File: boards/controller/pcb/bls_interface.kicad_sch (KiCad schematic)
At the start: 5 parts, among them J1101 PWM, J1102 SPI, J1103 Power

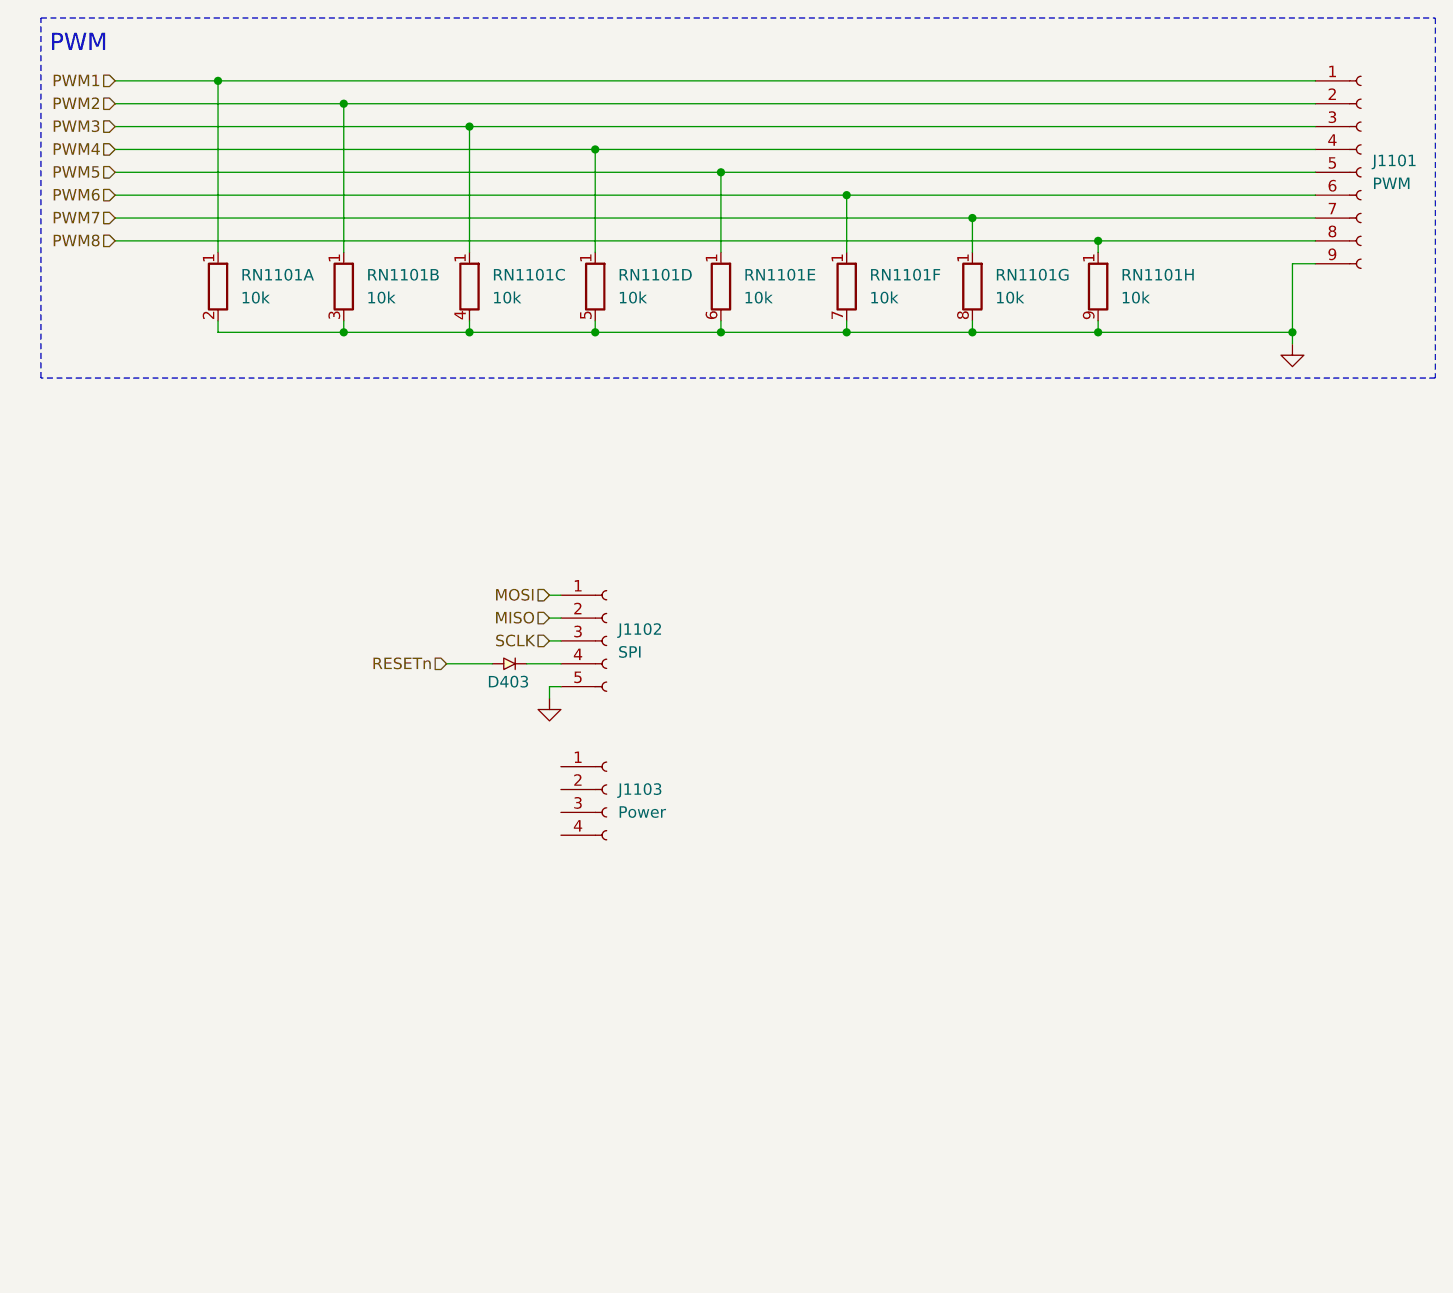
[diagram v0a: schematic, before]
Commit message: controller: pcb: Update schematic
Signed-off-by: Nicholas Loehrke <nicholasnloehrke@gmail.com>
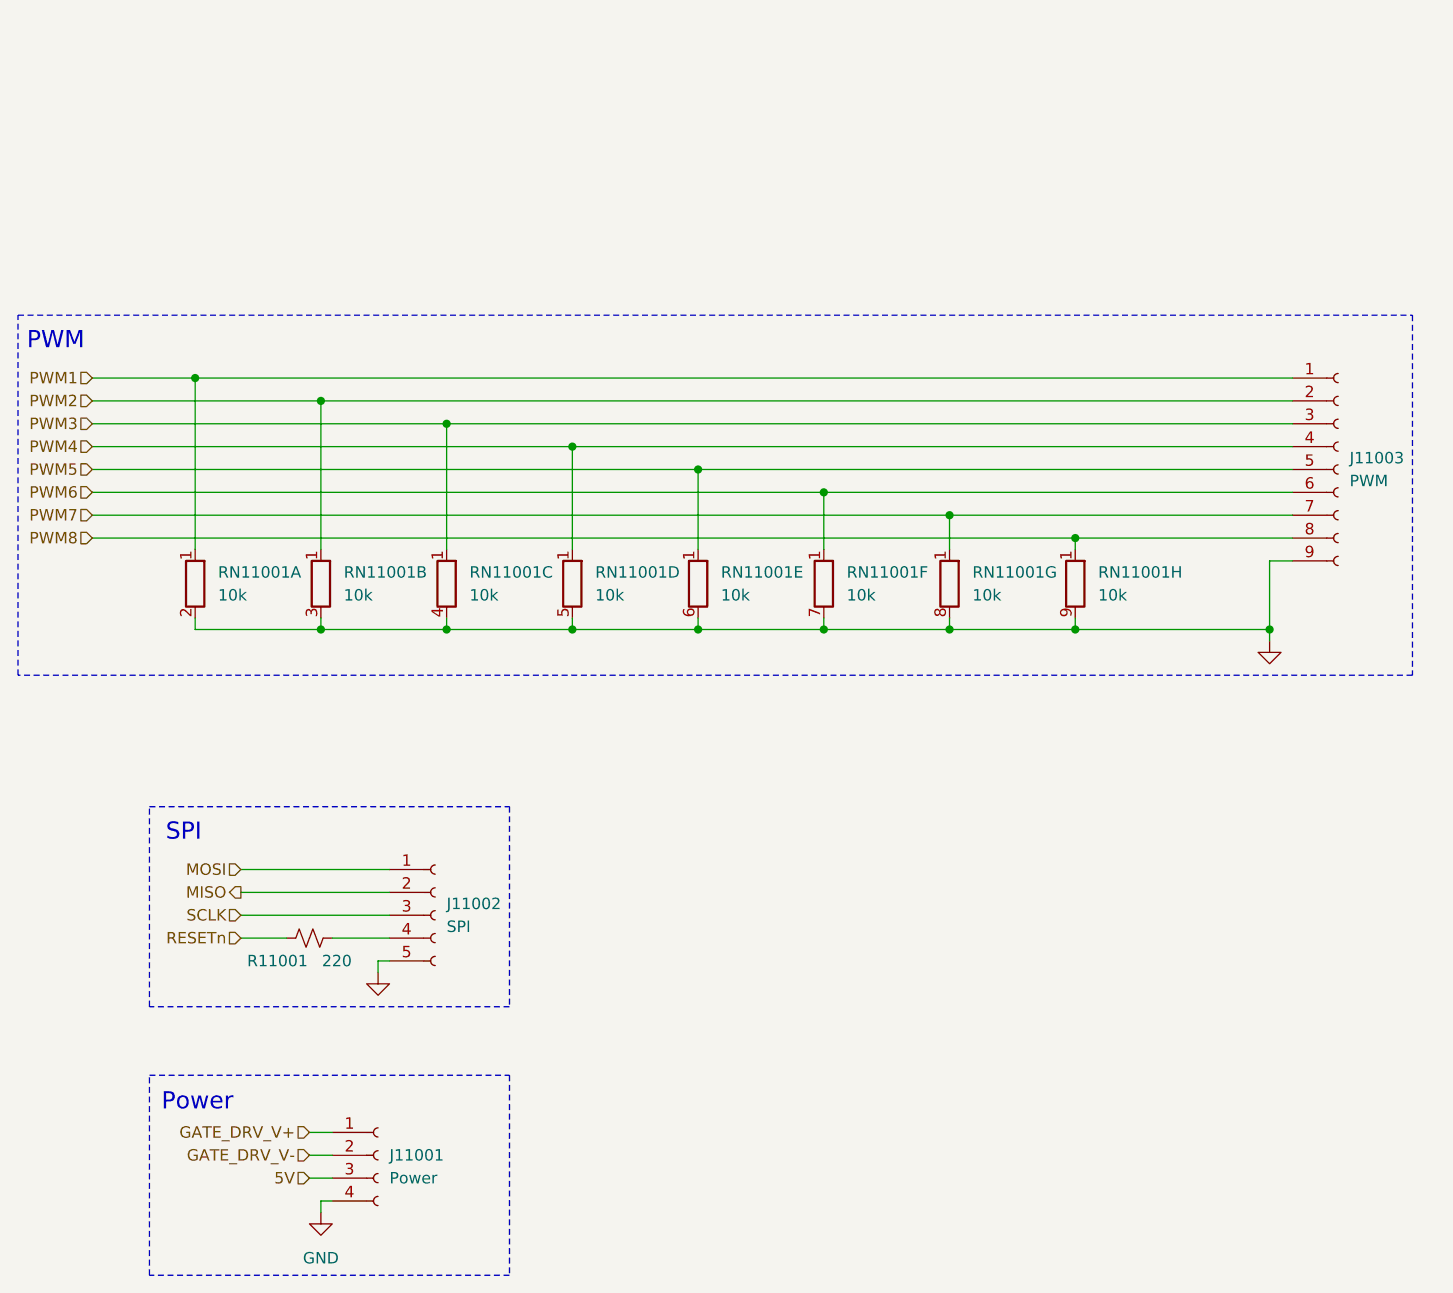
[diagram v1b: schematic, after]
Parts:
- removed D403: CUS10S30_H3F, USC_TOS, symbol CUS10S30_H3F:CUS10S30_H3F
- added R11001: 220, symbol Device:R_Small_US
- renumbered J1103 to J11001, J1102 to J11002, J1101 to J11003, RN1101 to RN11001
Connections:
- net GND: now also J11001.4 (Pin_4)
- net RESETn: now also R11001.1
- net GATE_DRV_V+: now reaches J11001.1 (Pin_1)
- net GATE_DRV_V-: now reaches J11001.2 (Pin_2)
- net 5V: now reaches J11001.3 (Pin_3)
- net at J11002.4 (Pin_4): now also R11001.2
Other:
- note added: "Power"
- note added: "SPI"
- moved on the sheet: J11001, J11002, J11003, RN11001A, RN11001B, RN11001C, RN11001D, RN11001E, RN11001F, RN11001G, RN11001H

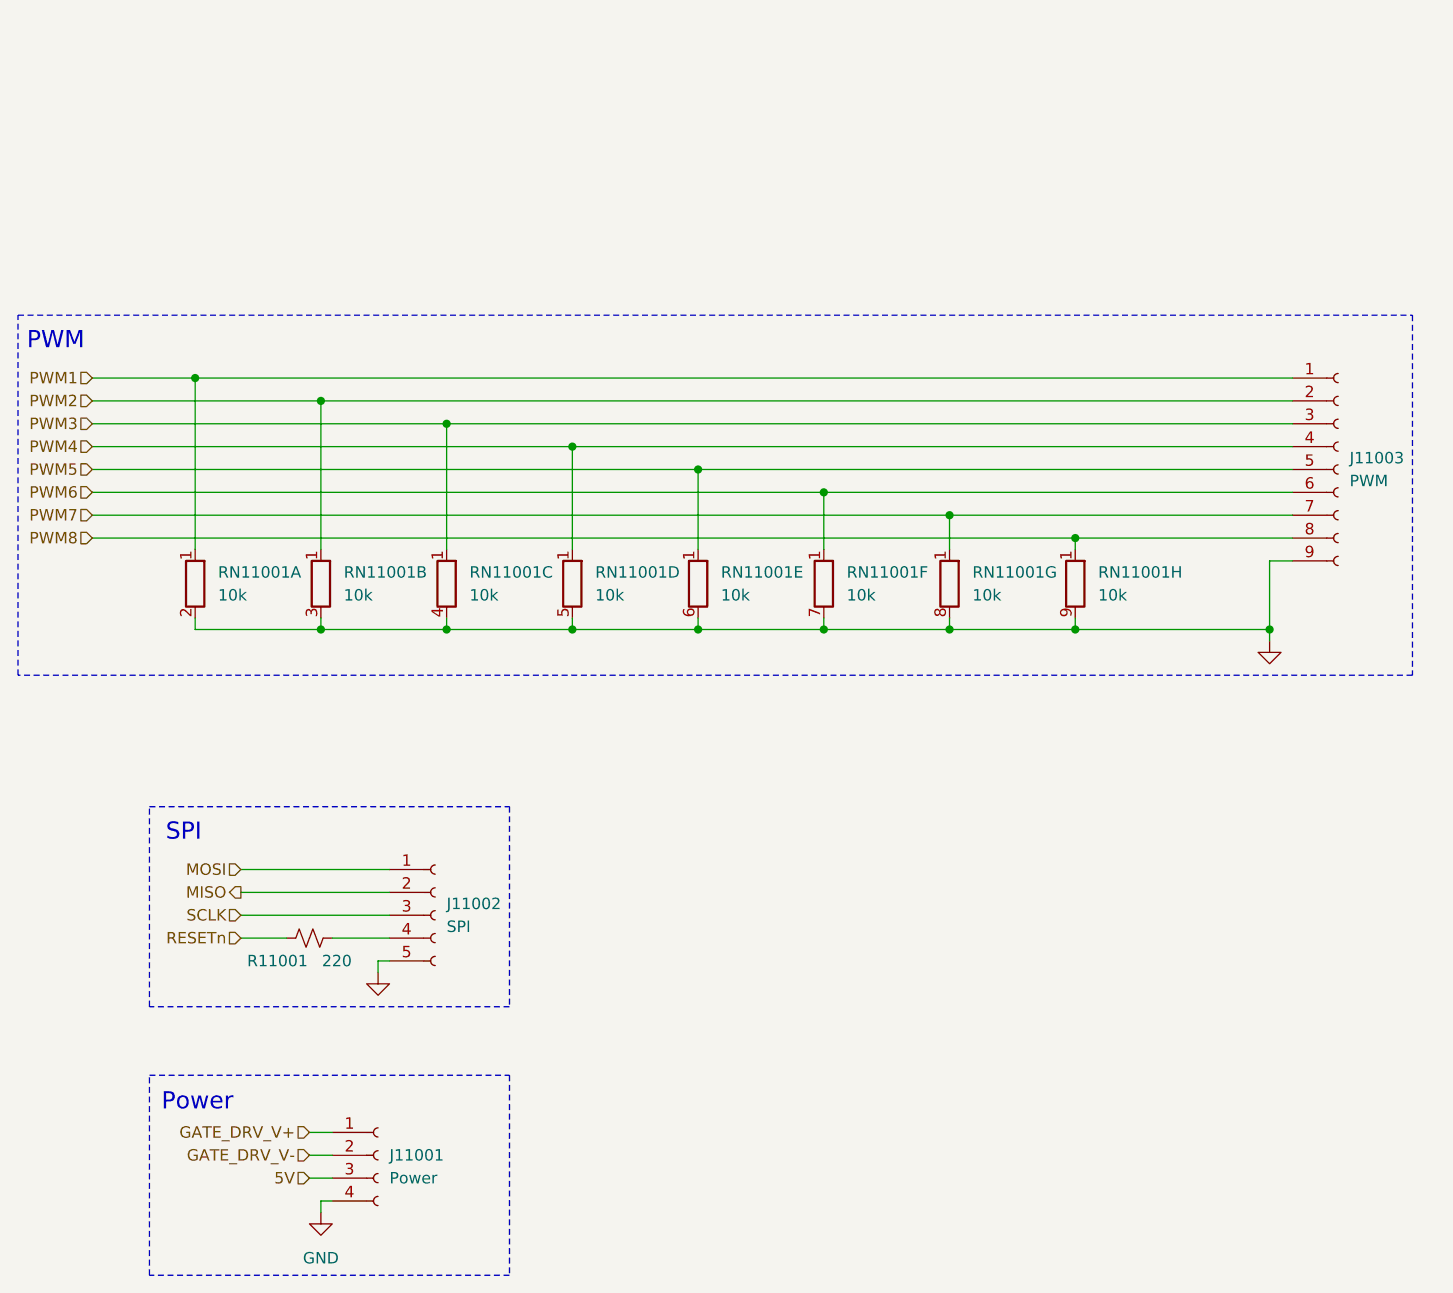
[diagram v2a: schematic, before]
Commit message: controller: pcb: Update schematic
- add VBAT sense circuit
- add BLS power pmos
- assign BLS GPIO

Signed-off-by: Nicholas Loehrke <nicholasnloehrke@gmail.com>
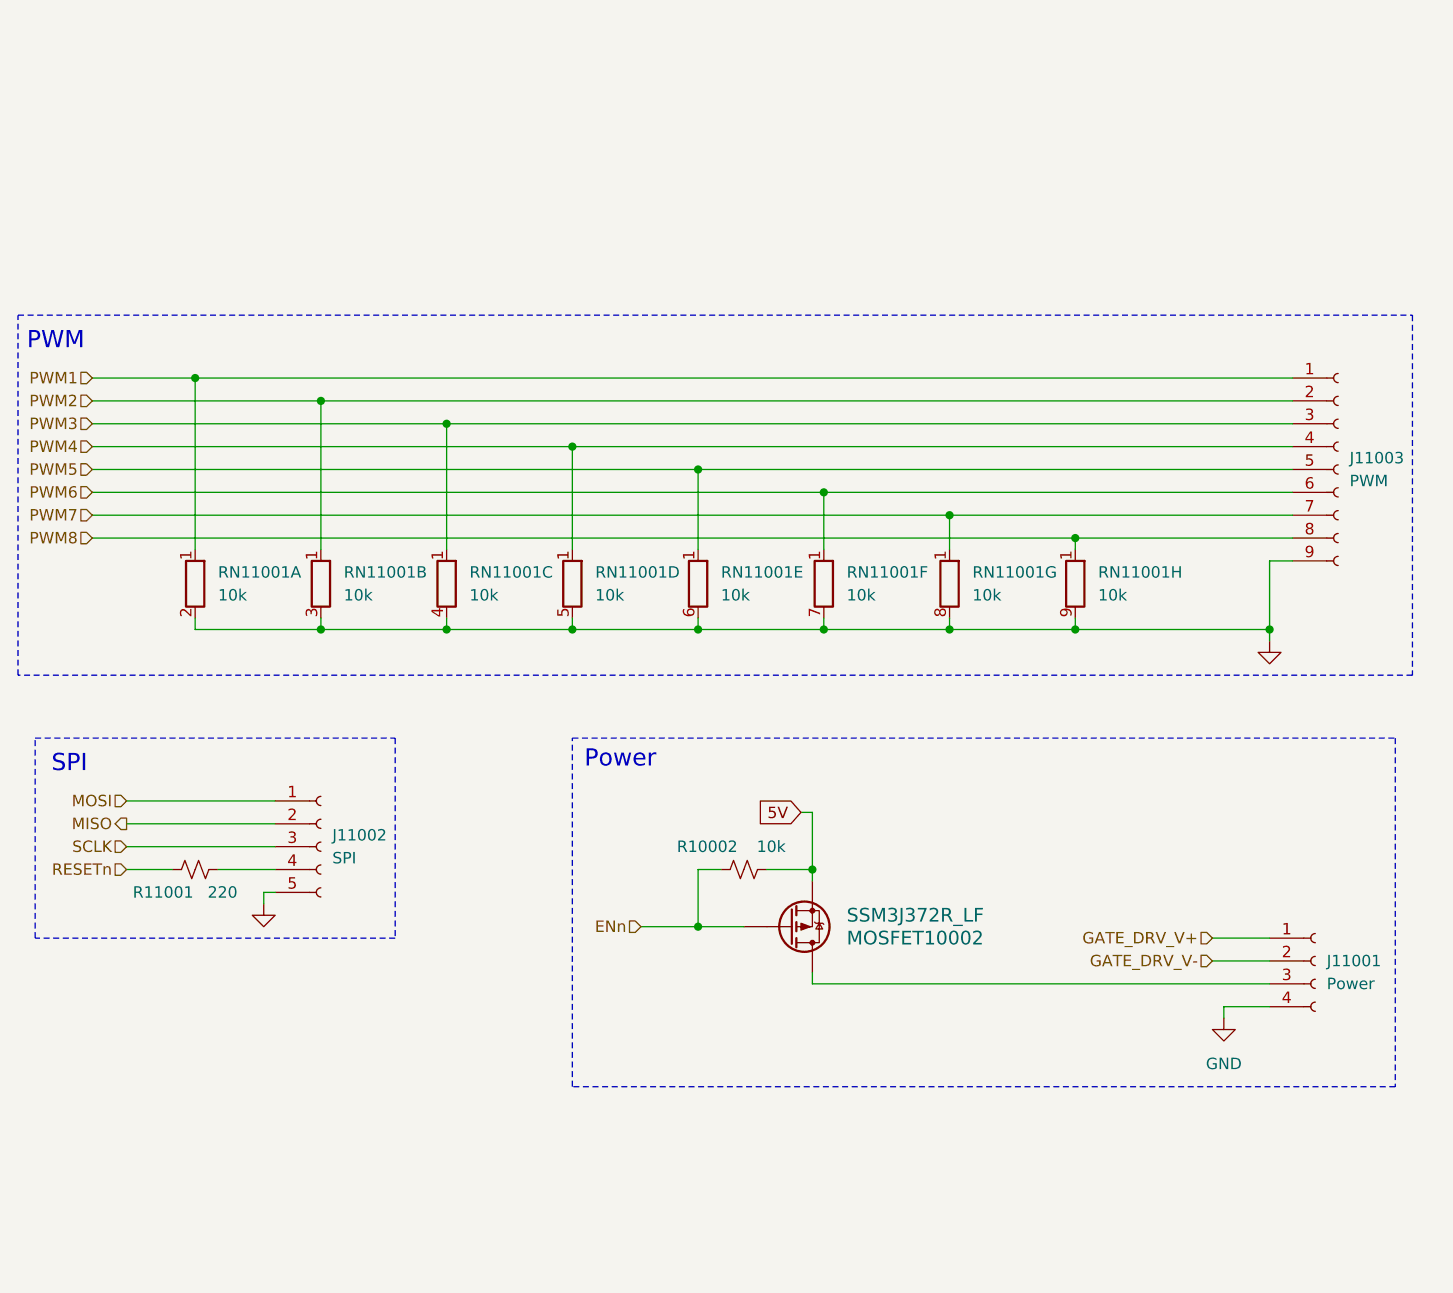
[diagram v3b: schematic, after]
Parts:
- added MOSFET10002: SSM3J372R_LF, SOT-23F_TOS, symbol SSM3J372R_LF:SSM3J372R_LF
- added R10002: 10k, symbol Device:R_Small_US
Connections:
- net 5V: now also MOSFET10002.2 (S), R10002.2; no longer J11001.3 (Pin_3)
- new net: J11001.3 (Pin_3), MOSFET10002.3 (D)
- new net ENn: MOSFET10002.1 (G), R10002.1
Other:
- moved on the sheet: J11001, J11002, R11001

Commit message: controller: pcb: Update schematic
Signed-off-by: Nicholas Loehrke <nicholasnloehrke@gmail.com>
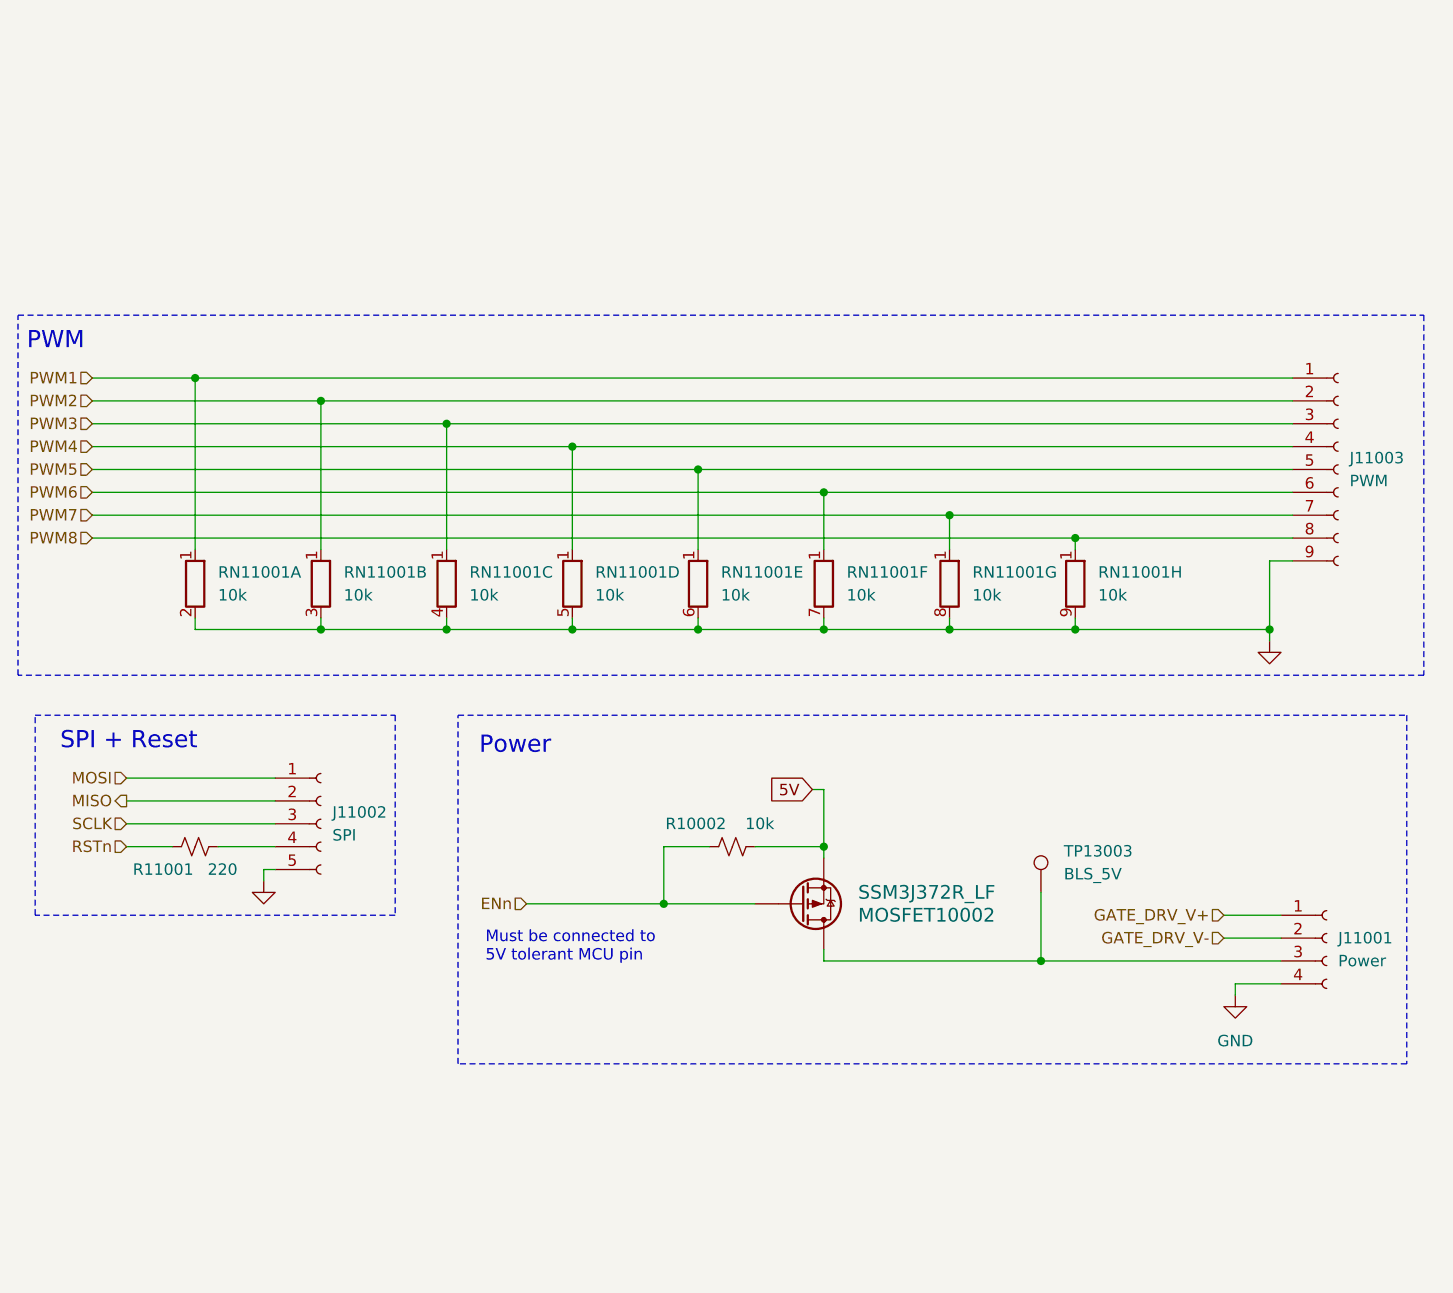
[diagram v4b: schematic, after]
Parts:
- added TP13003: BLS_5V, symbol Connector:TestPoint
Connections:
- net at J11001.3 (Pin_3), MOSFET10002.3 (D): now also TP13003.1
- net RESETn renamed RSTn
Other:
- note added: "Must be connected to 5V tolerant MCU pin"
- note added: "SPI + Reset"
- note removed: "SPI"
- moved on the sheet: J11001, J11002, MOSFET10002, R10002, R11001
